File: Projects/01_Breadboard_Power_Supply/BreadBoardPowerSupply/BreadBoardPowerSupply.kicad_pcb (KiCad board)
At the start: 2 copper layers, 30.1 x 52.1 mm, 15 parts, among them J1 Barrel_Jack_Switch, J2 Conn_02x02_Odd_Even, J3 Conn_02x02_Odd_Even, SW1 SW_DPDT_x2, U1 LM7805_TO220

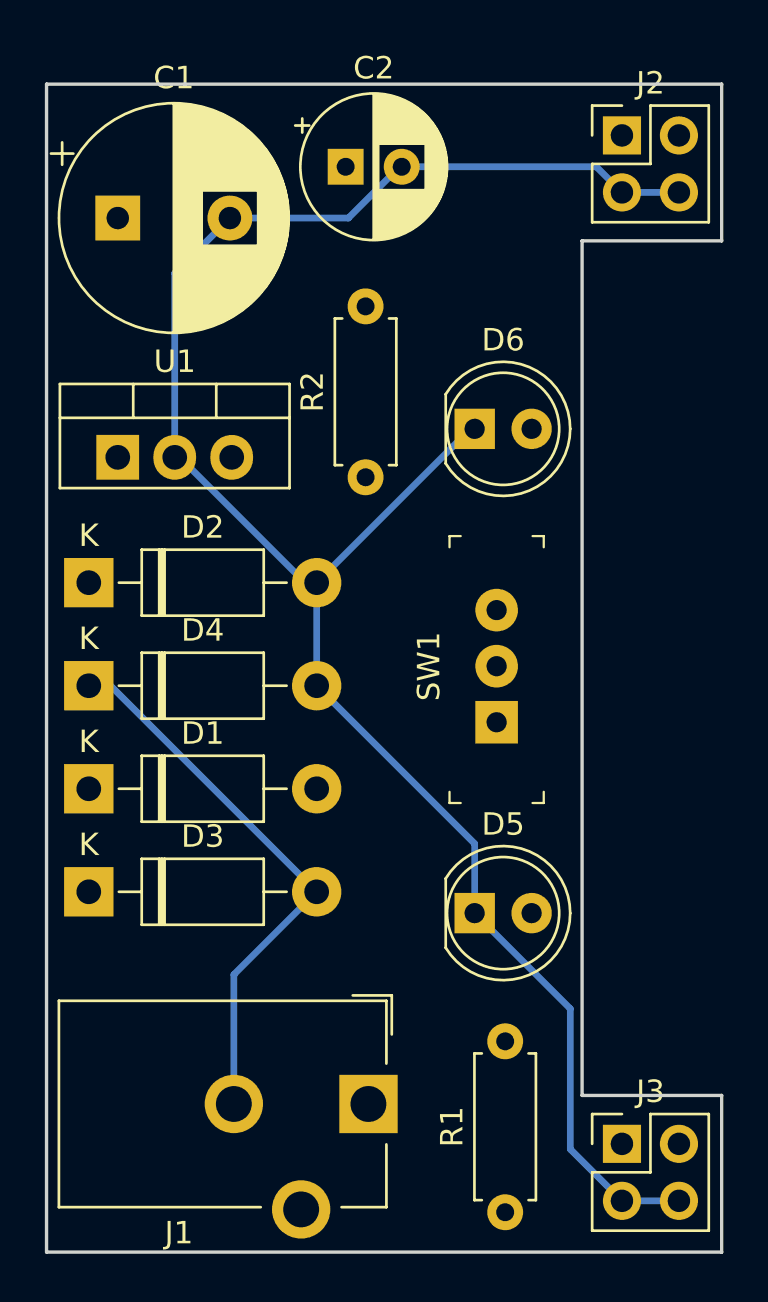
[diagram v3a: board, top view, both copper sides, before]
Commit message: Connect Vin traces on F.Cu and fix placement to allow traces to go along eges of board
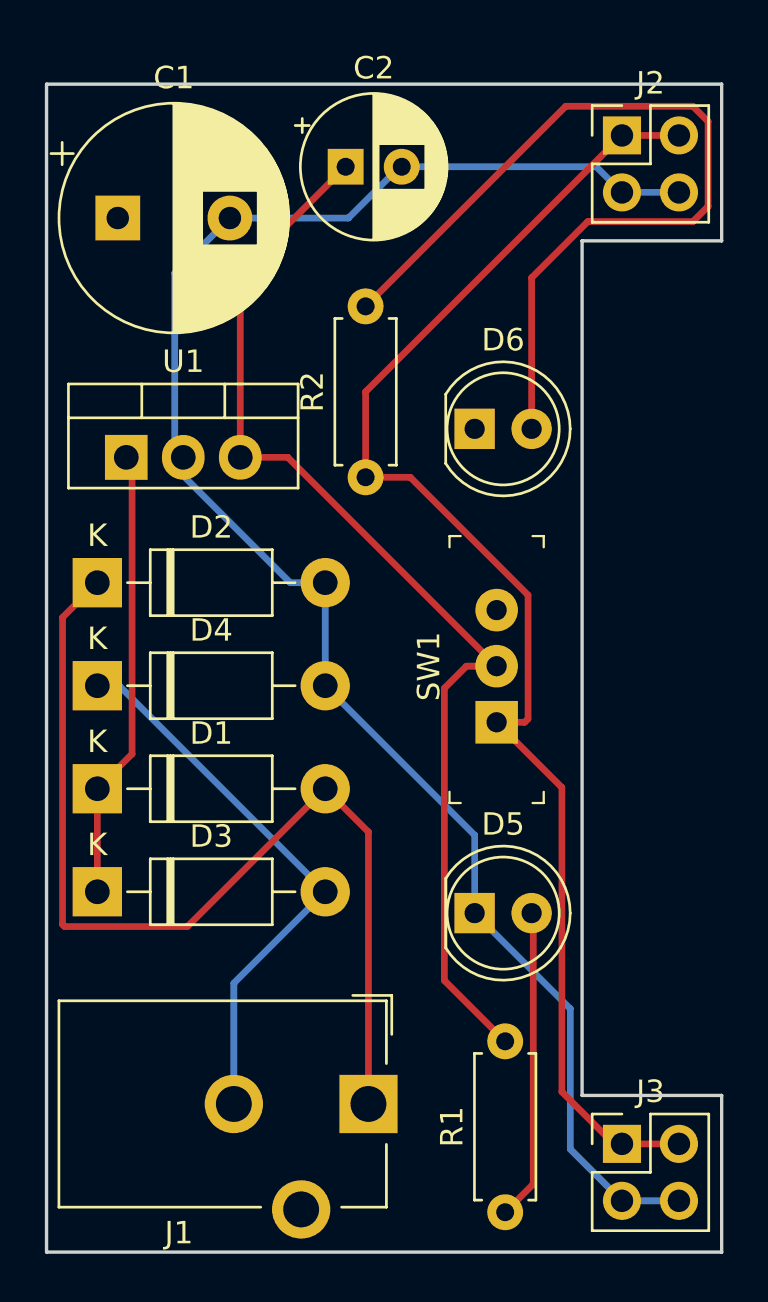
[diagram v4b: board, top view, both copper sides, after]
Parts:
- moved D1 0.38 mm to (125.6, 103.9)
- moved D2 0.38 mm to (125.6, 94.7)
- moved D3 0.38 mm to (125.6, 108.5)
- moved D4 0.38 mm to (125.6, 99.3)
- moved U1 0.38 mm to (126.9, 89.2)
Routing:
- net /Vout2: track 0.00 -> 62.8 mm
- net /Vout1: track 0.00 -> 49.8 mm
- net Net-(D1-Pad2): track 0.00 -> 45.0 mm
- net Net-(D6-Pad2): track 0.00 -> 39.0 mm
- net /Vin: track 0.36 -> 20.5 mm
- net Net-(D5-Pad2): track 0.00 -> 13.9 mm
- net /V-: track 87.4 -> 78.8 mm
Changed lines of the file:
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@@
     (thickness 1.6)
     (drawings 8)
-    (tracks 26)
+    (tracks 70)
     (zones 0)
     (modules 15)
@@
   )
   (module Diode_THT:D_DO-41_SOD81_P10.16mm_Horizontal (layer F.Cu)
-    (at 125.200001 103.929334)
+    (at 125.581001 103.929334)
     (descr "Diode, DO-41_SOD81 series, Axial, Horizontal, pin pitch=10.16mm, , length*diameter=5.2*2.7mm^2, , http://www.diodes.com/_files/packages/DO-41%20(Plastic).pdf")
     (tags "Diode DO-41_SOD81 series Axial Horizontal pin pitch 10.16mm  length 5.2mm diameter 2.7mm")
@@
   )
   (module Diode_THT:D_DO-41_SOD81_P10.16mm_Horizontal (layer F.Cu)
-    (at 125.200001 94.742)
+    (at 125.581001 94.742)
     (descr "Diode, DO-41_SOD81 series, Axial, Horizontal, pin pitch=10.16mm, , length*diameter=5.2*2.7mm^2, , http://www.diodes.com/_files/packages/DO-41%20(Plastic).pdf")
     (tags "Diode DO-41_SOD81 series Axial Horizontal pin pitch 10.16mm  length 5.2mm diameter 2.7mm")
@@
   )
   (module Diode_THT:D_DO-41_SOD81_P10.16mm_Horizontal (layer F.Cu)
-    (at 125.200001 108.523001)
+    (at 125.581001 108.523001)
     (descr "Diode, DO-41_SOD81 series, Axial, Horizontal, pin pitch=10.16mm, , length*diameter=5.2*2.7mm^2, , http://www.diodes.com/_files/packages/DO-41%20(Plastic).pdf")
     (tags "Diode DO-41_SOD81 series Axial Horizontal pin pitch 10.16mm  length 5.2mm diameter 2.7mm")
@@
   )
   (module Diode_THT:D_DO-41_SOD81_P10.16mm_Horizontal (layer F.Cu)
-    (at 125.200001 99.335667)
+    (at 125.581001 99.335667)
     (descr "Diode, DO-41_SOD81 series, Axial, Horizontal, pin pitch=10.16mm, , length*diameter=5.2*2.7mm^2, , http://www.diodes.com/_files/packages/DO-41%20(Plastic).pdf")
     (tags "Diode DO-41_SOD81 series Axial Horizontal pin pitch 10.16mm  length 5.2mm diameter 2.7mm")
@@
   )
   (module Package_TO_SOT_THT:TO-220-3_Vertical (layer F.Cu)
-    (at 126.492 89.154)
+    (at 126.873 89.154)
     (descr "TO-220-3, Vertical, RM 2.54mm, see https://www.vishay.com/docs/66542/to-220-1.pdf")
     (tags "TO-220-3 Vertical RM 2.54mm")
@@
   (gr_line (start 123.317 72.517) (end 123.317 124.587) (layer Edge.Cuts) (width 0.15))
   (segment (start 126.750002 89.412002) (end 126.492 89.154) (width 0.3) (layer F.Cu) (net 1))
-  (segment (start 135.360001 99.335667) (end 135.360001 94.742) (width 0.3) (layer B.Cu) (net 2))
+  (segment (start 125.581001 108.523001) (end 125.581001 103.929334) (width 0.3) (layer F.Cu) (net 1))
+  (segment (start 127.131002 89.412002) (end 126.873 89.154) (width 0.3) (layer F.Cu) (net 1))
+  (segment (start 127.131002 102.379333) (end 127.131002 89.412002) (width 0.3) (layer F.Cu) (net 1))
+  (segment (start 125.581001 103.929334) (end 127.131002 102.379333) (width 0.3) (layer F.Cu) (net 1))
   (segment (start 142.345001 87.757) (end 142.403 87.757) (width 0.3) (layer B.Cu) (net 2))
   (segment (start 129.254502 89.154) (end 129.032 89.154) (width 0.3) (layer B.Cu) (net 2))
-  (segment (start 134.842502 94.742) (end 129.254502 89.154) (width 0.3) (layer B.Cu) (net 2))
-  (segment (start 135.360001 94.742) (end 134.842502 94.742) (width 0.3) (layer B.Cu) (net 2))
+  (segment (start 135.741001 94.742) (end 135.223502 94.742) (width 0.3) (layer B.Cu) (net 2))
   (segment (start 129.032 80.946) (end 131.492 78.486) (width 0.3) (layer B.Cu) (net 2))
   (segment (start 129.032 89.154) (end 129.032 80.946) (width 0.3) (layer B.Cu) (net 2))
@@
   (segment (start 146.66799 119.99799) (end 146.66799 113.73899) (width 0.3) (layer B.Cu) (net 2))
   (segment (start 148.971 122.301) (end 146.66799 119.99799) (width 0.3) (layer B.Cu) (net 2))
-  (segment (start 142.403 106.378666) (end 135.360001 99.335667) (width 0.3) (layer B.Cu) (net 2))
-  (segment (start 142.403 109.474) (end 142.403 106.378666) (width 0.3) (layer B.Cu) (net 2))
   (segment (start 142.218001 87.884) (end 142.403 87.884) (width 0.3) (layer B.Cu) (net 2))
-  (segment (start 135.360001 94.742) (end 142.218001 87.884) (width 0.3) (layer B.Cu) (net 2))
-  (segment (start 131.668 112.215002) (end 135.360001 108.523001) (width 0.3) (layer B.Cu) (net 5))
-  (segment (start 131.668 117.983) (end 131.668 112.215002) (width 0.3) (layer B.Cu) (net 5))
-  (segment (start 126.172667 99.335667) (end 125.200001 99.335667) (width 0.3) (layer B.Cu) (net 5))
-  (segment (start 135.360001 108.523001) (end 126.172667 99.335667) (width 0.3) (layer B.Cu) (net 5))
+  (segment (start 142.403 105.997666) (end 135.741001 99.335667) (width 0.3) (layer B.Cu) (net 2))
+  (segment (start 142.403 109.474) (end 142.403 105.997666) (width 0.3) (layer B.Cu) (net 2))
+  (segment (start 135.741001 99.335667) (end 135.741001 94.742) (width 0.3) (layer B.Cu) (net 2))
+  (segment (start 129.413 89.969633) (end 129.413 89.154) (width 0.3) (layer B.Cu) (net 2))
+  (segment (start 134.185367 94.742) (end 129.413 89.969633) (width 0.3) (layer B.Cu) (net 2))
+  (segment (start 135.741001 94.742) (end 134.185367 94.742) (width 0.3) (layer B.Cu) (net 2))
+  (segment (start 141.052999 112.477999) (end 143.764 115.189) (width 0.3) (layer F.Cu) (net 3))
+  (segment (start 141.052999 99.451499) (end 141.052999 112.477999) (width 0.3) (layer F.Cu) (net 3))
+  (segment (start 142.039498 98.465) (end 141.052999 99.451499) (width 0.3) (layer F.Cu) (net 3))
+  (segment (start 143.383 98.465) (end 142.039498 98.465) (width 0.3) (layer F.Cu) (net 3))
+  (segment (start 134.072 89.154) (end 131.953 89.154) (width 0.3) (layer F.Cu) (net 3))
+  (segment (start 143.383 98.465) (end 134.072 89.154) (width 0.3) (layer F.Cu) (net 3))
+  (segment (start 131.953 80.899) (end 131.953 89.154) (width 0.3) (layer F.Cu) (net 3))
+  (segment (start 136.652 76.2) (end 131.953 80.899) (width 0.3) (layer F.Cu) (net 3))
+  (segment (start 124.031 96.292001) (end 125.581001 94.742) (width 0.3) (layer F.Cu) (net 4))
+  (segment (start 124.031 109.983002) (end 124.031 96.292001) (width 0.3) (layer F.Cu) (net 4))
+  (segment (start 124.121 110.073002) (end 124.031 109.983002) (width 0.3) (layer F.Cu) (net 4))
+  (segment (start 129.597333 110.073002) (end 124.121 110.073002) (width 0.3) (layer F.Cu) (net 4))
+  (segment (start 135.741001 103.929334) (end 129.597333 110.073002) (width 0.3) (layer F.Cu) (net 4))
+  (segment (start 137.668 105.856333) (end 135.741001 103.929334) (width 0.3) (layer F.Cu) (net 4))
+  (segment (start 137.668 117.983) (end 137.668 105.856333) (width 0.3) (layer F.Cu) (net 4))
+  (segment (start 126.553667 99.335667) (end 125.581001 99.335667) (width 0.3) (layer B.Cu) (net 5))
+  (segment (start 135.741001 108.523001) (end 126.553667 99.335667) (width 0.3) (layer B.Cu) (net 5))
+  (segment (start 131.668 112.596002) (end 135.741001 108.523001) (width 0.3) (layer B.Cu) (net 5))
+  (segment (start 131.668 117.983) (end 131.668 112.596002) (width 0.3) (layer B.Cu) (net 5))
+  (segment (start 145.014001 121.558999) (end 145.014001 109.545001) (width 0.3) (layer F.Cu) (net 6))
+  (segment (start 145.014001 109.545001) (end 144.943 109.474) (width 0.3) (layer F.Cu) (net 6))
+  (segment (start 143.764 122.809) (end 145.014001 121.558999) (width 0.3) (layer F.Cu) (net 6))
+  (segment (start 144.943 81.150946) (end 144.943 87.884) (width 0.3) (layer F.Cu) (net 7))
+  (segment (start 147.450945 78.643001) (end 144.943 81.150946) (width 0.3) (layer F.Cu) (net 7))
+  (segment (start 152.135001 78.643001) (end 147.450945 78.643001) (width 0.3) (layer F.Cu) (net 7))
+  (segment (start 152.811001 77.967001) (end 152.135001 78.643001) (width 0.3) (layer F.Cu) (net 7))
+  (segment (start 152.811001 74.178999) (end 152.811001 77.967001) (width 0.3) (layer F.Cu) (net 7))
+  (segment (start 152.135001 73.502999) (end 152.811001 74.178999) (width 0.3) (layer F.Cu) (net 7))
+  (segment (start 146.461001 73.502999) (end 152.135001 73.502999) (width 0.3) (layer F.Cu) (net 7))
+  (segment (start 137.541 82.423) (end 146.461001 73.502999) (width 0.3) (layer F.Cu) (net 7))
+  (segment (start 151.511 119.761) (end 148.971 119.761) (width 0.3) (layer F.Cu) (net 9))
+  (segment (start 146.293001 103.875001) (end 143.383 100.965) (width 0.3) (layer F.Cu) (net 9))
+  (segment (start 146.293001 117.444477) (end 146.293001 103.875001) (width 0.3) (layer F.Cu) (net 9))
+  (segment (start 148.609524 119.761) (end 146.293001 117.444477) (width 0.3) (layer F.Cu) (net 9))
+  (segment (start 148.971 119.761) (end 148.609524 119.761) (width 0.3) (layer F.Cu) (net 9))
+  (segment (start 144.783001 95.292999) (end 139.533002 90.043) (width 0.3) (layer F.Cu) (net 9))
+  (segment (start 144.783001 100.814999) (end 144.783001 95.292999) (width 0.3) (layer F.Cu) (net 9))
+  (segment (start 139.533002 90.043) (end 137.541 90.043) (width 0.3) (layer F.Cu) (net 9))
+  (segment (start 144.633 100.965) (end 144.783001 100.814999) (width 0.3) (layer F.Cu) (net 9))
+  (segment (start 143.383 100.965) (end 144.633 100.965) (width 0.3) (layer F.Cu) (net 9))
+  (segment (start 148.971 74.803) (end 151.511 74.803) (width 0.3) (layer F.Cu) (net 9))
+  (segment (start 137.541 86.233) (end 137.541 90.043) (width 0.3) (layer F.Cu) (net 9))
+  (segment (start 148.971 74.803) (end 137.541 86.233) (width 0.3) (layer F.Cu) (net 9))
 )

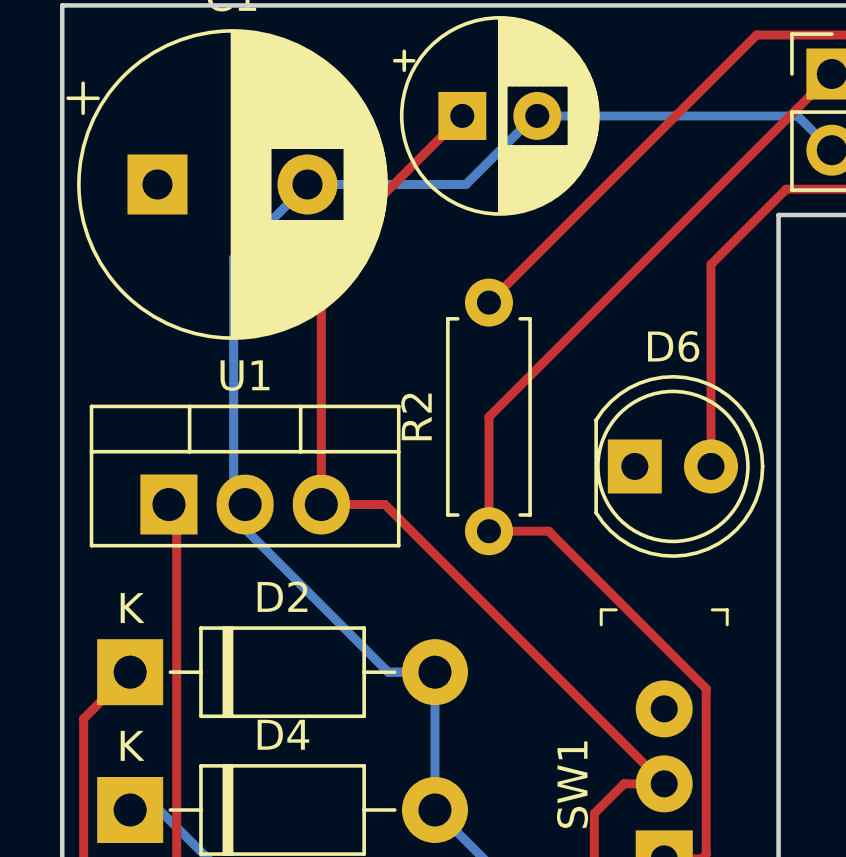
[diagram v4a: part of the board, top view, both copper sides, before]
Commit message: Run DRC and fix unconnected items: 	- D2 unconnected V- B.Cu 	- C1 unconnected Vin F.Cu
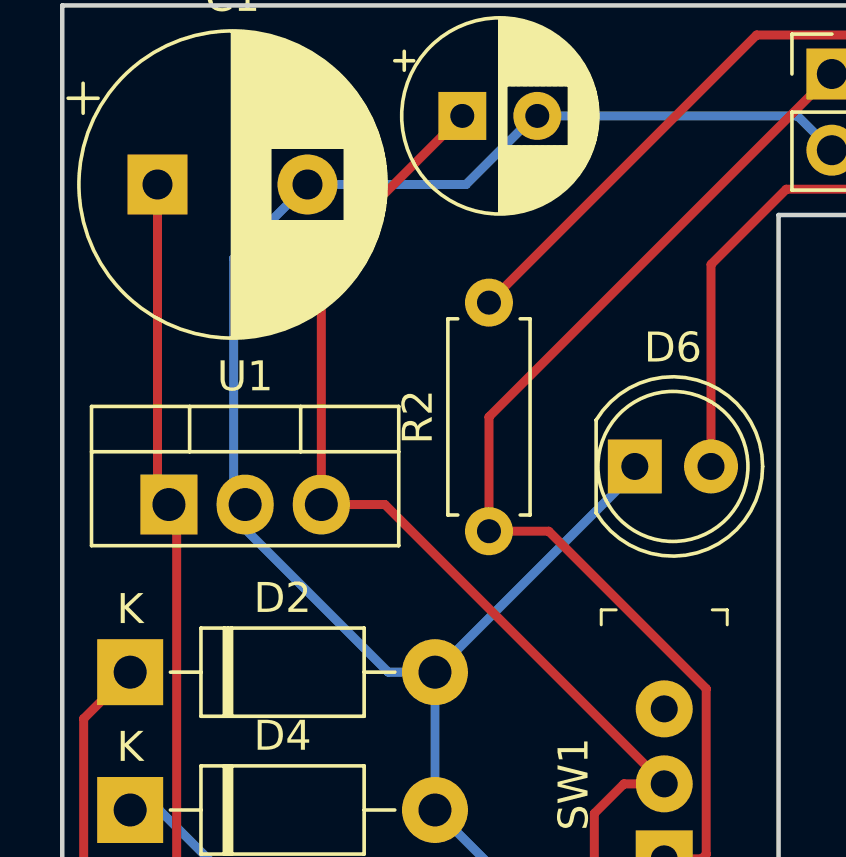
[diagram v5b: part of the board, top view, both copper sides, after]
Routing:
- net /Vin: track 20.5 -> 31.3 mm
- net /V-: track 78.8 -> 88.4 mm
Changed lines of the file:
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@@
     (thickness 1.6)
     (drawings 8)
-    (tracks 70)
+    (tracks 74)
     (zones 0)
     (modules 15)
@@
   (segment (start 127.131002 102.379333) (end 127.131002 89.412002) (width 0.3) (layer F.Cu) (net 1))
   (segment (start 125.581001 103.929334) (end 127.131002 102.379333) (width 0.3) (layer F.Cu) (net 1))
+  (segment (start 126.492 88.773) (end 126.873 89.154) (width 0.3) (layer F.Cu) (net 1))
+  (segment (start 126.492 78.486) (end 126.492 88.773) (width 0.3) (layer F.Cu) (net 1))
   (segment (start 142.345001 87.757) (end 142.403 87.757) (width 0.3) (layer B.Cu) (net 2))
   (segment (start 129.254502 89.154) (end 129.032 89.154) (width 0.3) (layer B.Cu) (net 2))
@@
   (segment (start 134.185367 94.742) (end 129.413 89.969633) (width 0.3) (layer B.Cu) (net 2))
   (segment (start 135.741001 94.742) (end 134.185367 94.742) (width 0.3) (layer B.Cu) (net 2))
+  (segment (start 142.403 88.080001) (end 135.741001 94.742) (width 0.3) (layer B.Cu) (net 2))
+  (segment (start 142.403 87.884) (end 142.403 88.080001) (width 0.3) (layer B.Cu) (net 2))
   (segment (start 141.052999 112.477999) (end 143.764 115.189) (width 0.3) (layer F.Cu) (net 3))
   (segment (start 141.052999 99.451499) (end 141.052999 112.477999) (width 0.3) (layer F.Cu) (net 3))
